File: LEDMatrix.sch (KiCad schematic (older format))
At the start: 80 parts

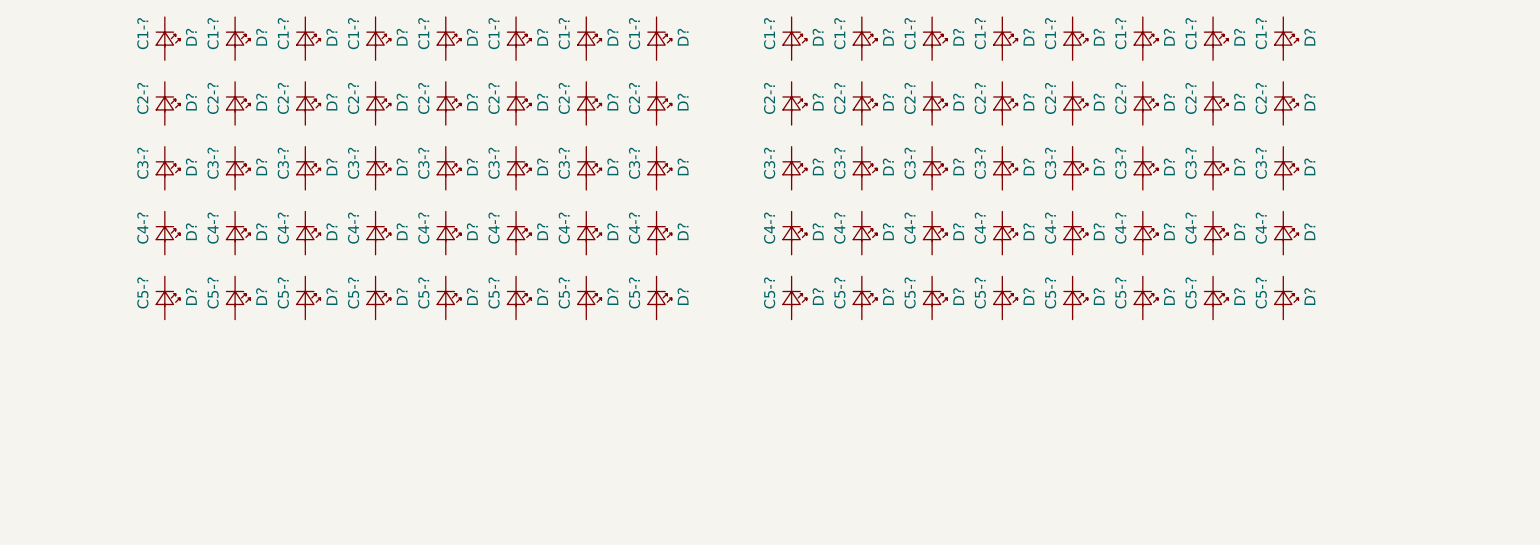
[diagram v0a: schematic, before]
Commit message: Place and annotate LED schematic components
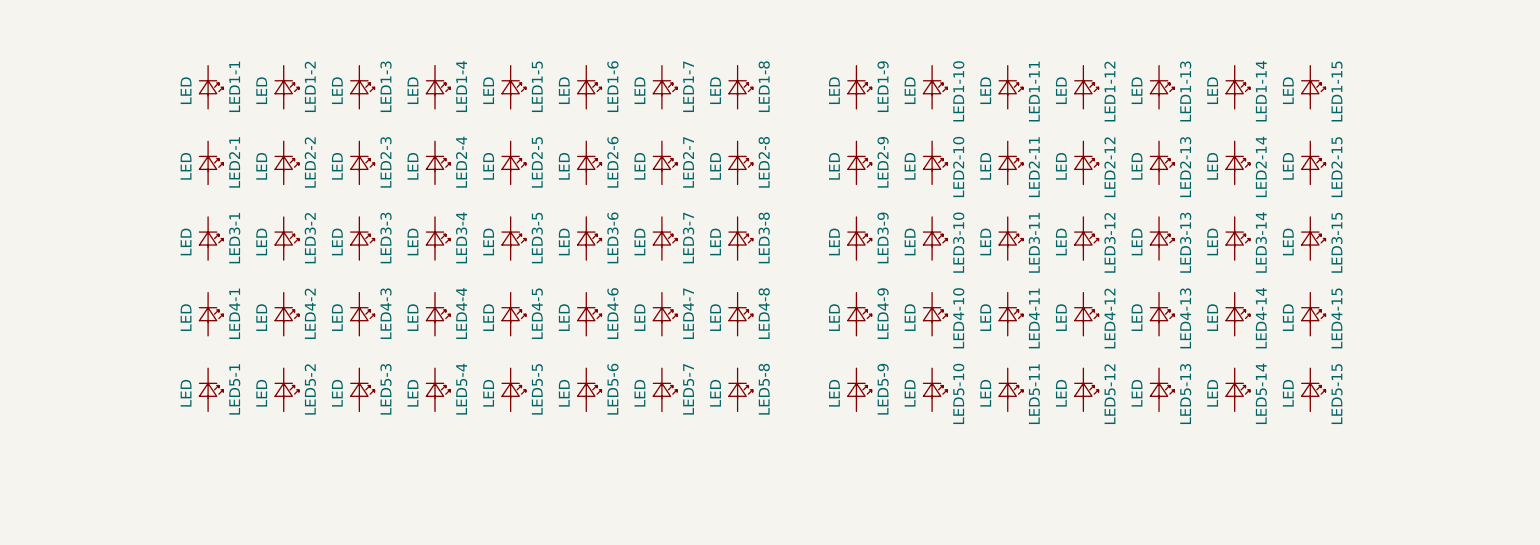
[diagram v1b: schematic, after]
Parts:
- removed D? (x16): C1-?, symbol LED_Small
- removed D? (x16): C2-?, symbol LED_Small
- removed D? (x16): C3-?, symbol LED_Small
- removed D? (x16): C4-?, symbol LED_Small
- removed D? (x16): C5-?, symbol LED_Small
- added LED1-1, LED1-10, LED1-11, LED1-12, LED1-13, LED1-14, LED1-15, LED1-2, LED1-3, LED1-4, LED1-5, LED1-6, LED1-7, LED1-8, LED1-9, LED2-1, LED2-10, LED2-11, LED2-12, LED2-13, LED2-14, LED2-15, LED2-2, LED2-3, LED2-4, LED2-5, LED2-6, LED2-7, LED2-8, LED2-9, LED3-1, LED3-10, LED3-11, LED3-12, LED3-13, LED3-14, LED3-15, LED3-2, LED3-3, LED3-4, LED3-5, LED3-6, LED3-7, LED3-8, LED3-9, LED4-1, LED4-10, LED4-11, LED4-12, LED4-13, LED4-14, LED4-15, LED4-2, LED4-3, LED4-4, LED4-5, LED4-6, LED4-7, LED4-8, LED4-9, LED5-1, LED5-10, LED5-11, LED5-12, LED5-13, LED5-14, LED5-15, LED5-2, LED5-3, LED5-4, LED5-5, LED5-6, LED5-7, LED5-8, LED5-9: LED, symbol LED_Small

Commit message: Wire lefthand matrix schematic
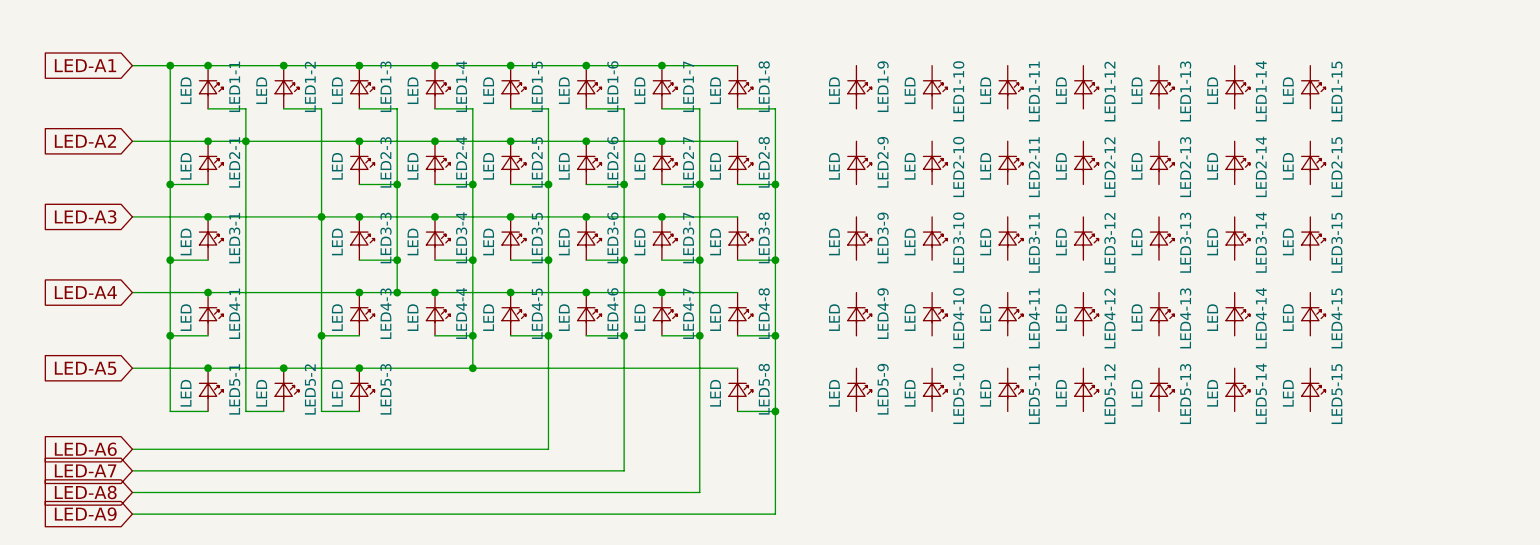
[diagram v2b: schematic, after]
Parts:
- removed LED2-2, LED3-2, LED4-2, LED5-4, LED5-5, LED5-6, LED5-7: LED, symbol LED_Small
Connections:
- net LED-A1: now reaches LED1-1.1 (K)
- net LED-A1: now also LED1-2.1 (K), LED1-3.1 (K), LED1-4.1 (K), LED1-5.1 (K), LED1-6.1 (K), LED1-7.1 (K), LED1-8.1 (K), LED2-1.2 (A), LED3-1.2 (A), LED4-1.2 (A), LED5-1.2 (A)
- net LED-A2: now reaches LED1-1.2 (A)
- net LED-A2: now also LED2-1.1 (K), LED2-3.1 (K), LED2-4.1 (K), LED2-5.1 (K), LED2-6.1 (K), LED2-7.1 (K), LED2-8.1 (K), LED5-2.2 (A)
- net LED-A3: now reaches LED1-2.2 (A)
- net LED-A3: now also LED3-1.1 (K), LED3-3.1 (K), LED3-4.1 (K), LED3-5.1 (K), LED3-6.1 (K), LED3-7.1 (K), LED3-8.1 (K), LED4-3.2 (A), LED5-3.2 (A)
- net LED-A4: now reaches LED1-3.2 (A)
- net LED-A4: now also LED2-3.2 (A), LED3-3.2 (A), LED4-1.1 (K), LED4-3.1 (K), LED4-4.1 (K), LED4-5.1 (K), LED4-6.1 (K), LED4-7.1 (K), LED4-8.1 (K)
- net LED-A5: now reaches LED1-4.2 (A)
- net LED-A5: now also LED2-4.2 (A), LED3-4.2 (A), LED4-4.2 (A), LED5-1.1 (K), LED5-2.1 (K), LED5-3.1 (K), LED5-8.1 (K)
- net LED-A6: now reaches LED1-5.2 (A)
- net LED-A6: now also LED2-5.2 (A), LED3-5.2 (A), LED4-5.2 (A)
- net LED-A7: now reaches LED1-6.2 (A)
- net LED-A7: now also LED2-6.2 (A), LED3-6.2 (A), LED4-6.2 (A)
- net LED-A8: now reaches LED1-7.2 (A)
- net LED-A8: now also LED2-7.2 (A), LED3-7.2 (A), LED4-7.2 (A)
- net LED-A9: now reaches LED1-8.2 (A)
- net LED-A9: now also LED2-8.2 (A), LED3-8.2 (A), LED4-8.2 (A), LED5-8.2 (A)

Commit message: Wire righthand matrix
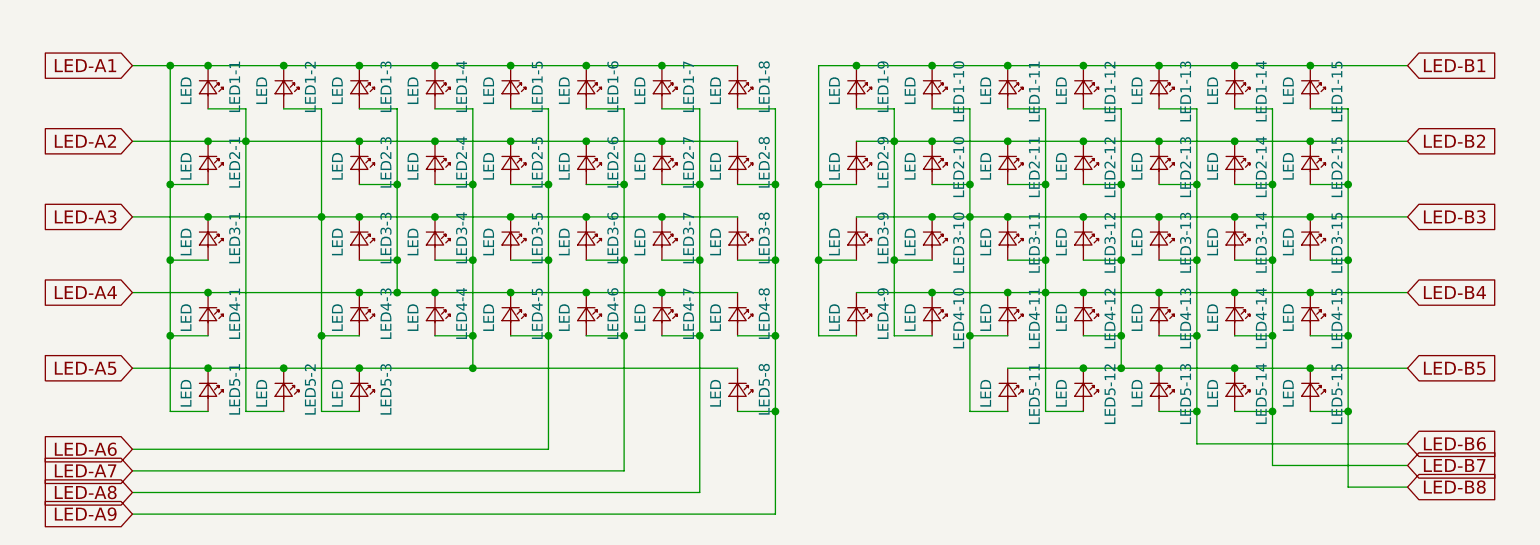
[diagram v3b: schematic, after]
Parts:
- removed LED5-10, LED5-9: LED, symbol LED_Small
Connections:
- net LED-B1: now reaches LED1-9.1 (K)
- net LED-B1: now also LED1-10.1 (K), LED1-11.1 (K), LED1-12.1 (K), LED1-13.1 (K), LED1-14.1 (K), LED1-15.1 (K), LED2-9.2 (A), LED3-9.2 (A), LED4-9.2 (A)
- net LED-B2: now reaches LED1-9.2 (A)
- net LED-B2: now also LED2-10.1 (K), LED2-11.1 (K), LED2-12.1 (K), LED2-13.1 (K), LED2-14.1 (K), LED2-15.1 (K), LED2-9.1 (K), LED3-10.2 (A), LED4-10.2 (A)
- net LED-B3: now reaches LED1-10.2 (A)
- net LED-B3: now also LED2-10.2 (A), LED3-10.1 (K), LED3-11.1 (K), LED3-12.1 (K), LED3-13.1 (K), LED3-14.1 (K), LED3-15.1 (K), LED3-9.1 (K), LED4-11.2 (A), LED5-11.2 (A)
- net LED-B4: now reaches LED1-11.2 (A)
- net LED-B4: now also LED2-11.2 (A), LED3-11.2 (A), LED4-10.1 (K), LED4-11.1 (K), LED4-12.1 (K), LED4-13.1 (K), LED4-14.1 (K), LED4-15.1 (K), LED4-9.1 (K), LED5-12.2 (A)
- net LED-B5: now reaches LED1-12.2 (A)
- net LED-B5: now also LED2-12.2 (A), LED3-12.2 (A), LED4-12.2 (A), LED5-11.1 (K), LED5-12.1 (K), LED5-13.1 (K), LED5-14.1 (K), LED5-15.1 (K)
- net LED-B6: now reaches LED1-13.2 (A)
- net LED-B6: now also LED2-13.2 (A), LED3-13.2 (A), LED4-13.2 (A), LED5-13.2 (A)
- net LED-B7: now reaches LED1-14.2 (A)
- net LED-B7: now also LED2-14.2 (A), LED3-14.2 (A), LED4-14.2 (A), LED5-14.2 (A)
- net LED-B8: now reaches LED1-15.2 (A)
- net LED-B8: now also LED2-15.2 (A), LED3-15.2 (A), LED4-15.2 (A), LED5-15.2 (A)
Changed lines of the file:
@@
-$EndComp
-$Comp
-L LED_Small LED5-9
-U 1 1 5A6E1441
-P 5200 3350
-F 0 "LED5-9" H 5075 3475 50  0000 L CNN
-F 1 "LED" H 5150 3250 50  0000 L CNN
-F 2 "" V 5200 3350 50  0001 C CNN
-F 3 "" V 5200 3350 50  0001 C CNN
-	1    5200 3350
-	0    1    1    0
-$EndComp
-$Comp
-L LED_Small LED5-10
-U 1 1 5A6E1447
-P 5550 3350
-F 0 "LED5-10" H 5425 3475 50  0000 L CNN
-F 1 "LED" H 5500 3250 50  0000 L CNN
-F 2 "" V 5550 3350 50  0001 C CNN
-F 3 "" V 5550 3350 50  0001 C CNN
-	1    5550 3350
-	0    1    1    0
 $EndComp
 $Comp
@@
 Text GLabel 1850 3250 0    60   Input ~ 0
 LED-A5
+Text GLabel 1850 3625 0    60   Input ~ 0
+LED-A6
+Text GLabel 1850 3725 0    60   Input ~ 0
+LED-A7
+Text GLabel 1850 3825 0    60   Input ~ 0
+LED-A8
+Text GLabel 1850 3925 0    60   Input ~ 0
+LED-A9
+Text GLabel 7750 1850 2    60   Input ~ 0
+LED-B1
+Text GLabel 7750 2200 2    60   Input ~ 0
+LED-B2
+Text GLabel 7750 2550 2    60   Input ~ 0
+LED-B3
+Text GLabel 7750 2900 2    60   Input ~ 0
+LED-B4
+Text GLabel 7750 3250 2    60   Input ~ 0
+LED-B5
 Wire Wire Line
 	1850 1850 4650 1850
@@
 	3425 2050 3250 2050
 Connection ~ 3425 2400
-Text GLabel 1850 3625 0    60   Input ~ 0
-LED-A6
 Wire Wire Line
 	3775 3625 1850 3625
@@
 	3775 2050 3600 2050
 Connection ~ 3775 2400
-Text GLabel 1850 3725 0    60   Input ~ 0
-LED-A7
 Wire Wire Line
 	4125 3725 1850 3725
@@
 	4125 2050 3950 2050
 Connection ~ 4125 2400
-Text GLabel 1850 3825 0    60   Input ~ 0
-LED-A8
 Wire Wire Line
 	4475 3825 1850 3825
@@
 	4475 2050 4300 2050
 Connection ~ 4475 2400
-Text GLabel 1850 3925 0    60   Input ~ 0
-LED-A9
 Wire Wire Line
 	4825 3925 1850 3925
@@
 	4825 2050 4650 2050
 Connection ~ 4825 2400
+Wire Wire Line
+	5025 1850 7750 1850
+Connection ~ 5550 1850
+Connection ~ 5900 1850
+Connection ~ 6250 1850
+Connection ~ 6600 1850
+Connection ~ 6950 1850
+Connection ~ 7300 1850
+Wire Wire Line
+	5200 2200 7750 2200
+Connection ~ 5550 2200
+Connection ~ 5900 2200
+Connection ~ 6250 2200
+Connection ~ 6600 2200
+Connection ~ 6950 2200
+Connection ~ 7300 2200
+Wire Wire Line
+	5200 2550 7750 2550
+Connection ~ 5550 2550
+Connection ~ 5900 2550
+Connection ~ 6250 2550
+Connection ~ 6600 2550
+Connection ~ 6950 2550
+Connection ~ 7300 2550
+Wire Wire Line
+	5200 2900 7750 2900
+Connection ~ 5550 2900
+Connection ~ 5900 2900
+Connection ~ 6250 2900
+Connection ~ 6600 2900
+Connection ~ 6950 2900
+Connection ~ 7300 2900
+Wire Wire Line
+	5900 3250 7750 3250
+Connection ~ 6250 3250
+Connection ~ 6600 3250
+Connection ~ 6950 3250
+Connection ~ 7300 3250
+Wire Wire Line
+	5025 1850 5025 3100
+Wire Wire Line
+	5025 2400 5200 2400
+Connection ~ 5200 1850
+Wire Wire Line
+	5025 2750 5200 2750
+Connection ~ 5025 2400
+Wire Wire Line
+	5025 3100 5200 3100
+Connection ~ 5025 2750
+Wire Wire Line
+	5375 2050 5375 3100
+Wire Wire Line
+	5375 2050 5200 2050
+Connection ~ 5375 2200
+Wire Wire Line
+	5375 2750 5550 2750
+Wire Wire Line
+	5375 3100 5550 3100
+Connection ~ 5375 2750
+Wire Wire Line
+	5725 2050 5725 3450
+Wire Wire Line
+	5725 2400 5550 2400
+Connection ~ 5725 2550
+Wire Wire Line
+	5725 2050 5550 2050
+Connection ~ 5725 2400
+Wire Wire Line
+	5725 3100 5900 3100
+Wire Wire Line
+	5725 3450 5900 3450
+Connection ~ 5725 3100
+Wire Wire Line
+	6075 2050 6075 3450
+Wire Wire Line
+	6075 2750 5900 2750
+Connection ~ 6075 2900
+Wire Wire Line
+	6075 2400 5900 2400
+Connection ~ 6075 2750
+Wire Wire Line
+	6075 2050 5900 2050
+Connection ~ 6075 2400
+Wire Wire Line
+	6075 3450 6250 3450
+Wire Wire Line
+	6250 2050 6425 2050
+Wire Wire Line
+	6425 2050 6425 3250
+Connection ~ 6425 3250
+Wire Wire Line
+	6250 3100 6425 3100
+Connection ~ 6425 3100
+Wire Wire Line
+	6425 2750 6250 2750
+Connection ~ 6425 2750
+Wire Wire Line
+	6250 2400 6425 2400
+Connection ~ 6425 2400
+Wire Wire Line
+	6600 3100 6775 3100
+Wire Wire Line
+	6775 2050 6775 3600
+Wire Wire Line
+	6775 2750 6600 2750
+Wire Wire Line
+	6775 3450 6600 3450
+Connection ~ 6775 3100
+Wire Wire Line
+	6775 2400 6600 2400
+Connection ~ 6775 2750
+Wire Wire Line
+	6600 2050 6775 2050
+Connection ~ 6775 2400
+Wire Wire Line
+	6950 2050 7125 2050
+Wire Wire Line
+	7125 2050 7125 3700
+Wire Wire Line
+	7125 2400 6950 2400
+Wire Wire Line
+	7125 2750 6950 2750
+Connection ~ 7125 2400
+Wire Wire Line
+	7125 3100 6950 3100
+Connection ~ 7125 2750
+Wire Wire Line
+	7125 3450 6950 3450
+Connection ~ 7125 3100
+Wire Wire Line
+	7300 2050 7475 2050
+Wire Wire Line
+	7475 2050 7475 3800
+Wire Wire Line
+	7475 2400 7300 2400
+Wire Wire Line
+	7475 2750 7300 2750
+Connection ~ 7475 2400
+Wire Wire Line
+	7475 3100 7300 3100
+Connection ~ 7475 2750
+Wire Wire Line
+	7475 3450 7300 3450
+Connection ~ 7475 3100
+Wire Wire Line
+	6775 3600 7750 3600
+Connection ~ 6775 3450
+Text GLabel 7750 3600 2    60   Input ~ 0
+LED-B6
+Text GLabel 7750 3700 2    60   Input ~ 0
+LED-B7
+Wire Wire Line
+	7125 3700 7750 3700
+Connection ~ 7125 3450
+Text GLabel 7750 3800 2    60   Input ~ 0
+LED-B8
+Wire Wire Line
+	7475 3800 7750 3800
+Connection ~ 7475 3450
 $EndSCHEMATC

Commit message: Assign footprints
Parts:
- LED1-1, LED1-10, LED1-11, LED1-12, LED1-13, LED1-14, LED1-15, LED1-2, LED1-3, LED1-4, LED1-5, LED1-6, LED1-7, LED1-8, LED1-9, LED2-1, LED2-10, LED2-11, LED2-12, LED2-13, LED2-14, LED2-15, LED2-3, LED2-4, LED2-5, LED2-6, LED2-7, LED2-8, LED2-9, LED3-1, LED3-10, LED3-11, LED3-12, LED3-13, LED3-14, LED3-15, LED3-3, LED3-4, LED3-5, LED3-6, LED3-7, LED3-8, LED3-9, LED4-1, LED4-10, LED4-11, LED4-12, LED4-13, LED4-14, LED4-15, LED4-3, LED4-4, LED4-5, LED4-6, LED4-7, LED4-8, LED4-9, LED5-1, LED5-11, LED5-12, LED5-13, LED5-14, LED5-15, LED5-2, LED5-3, LED5-8: footprint (none) -> MX_Alps_Hybrid:LED

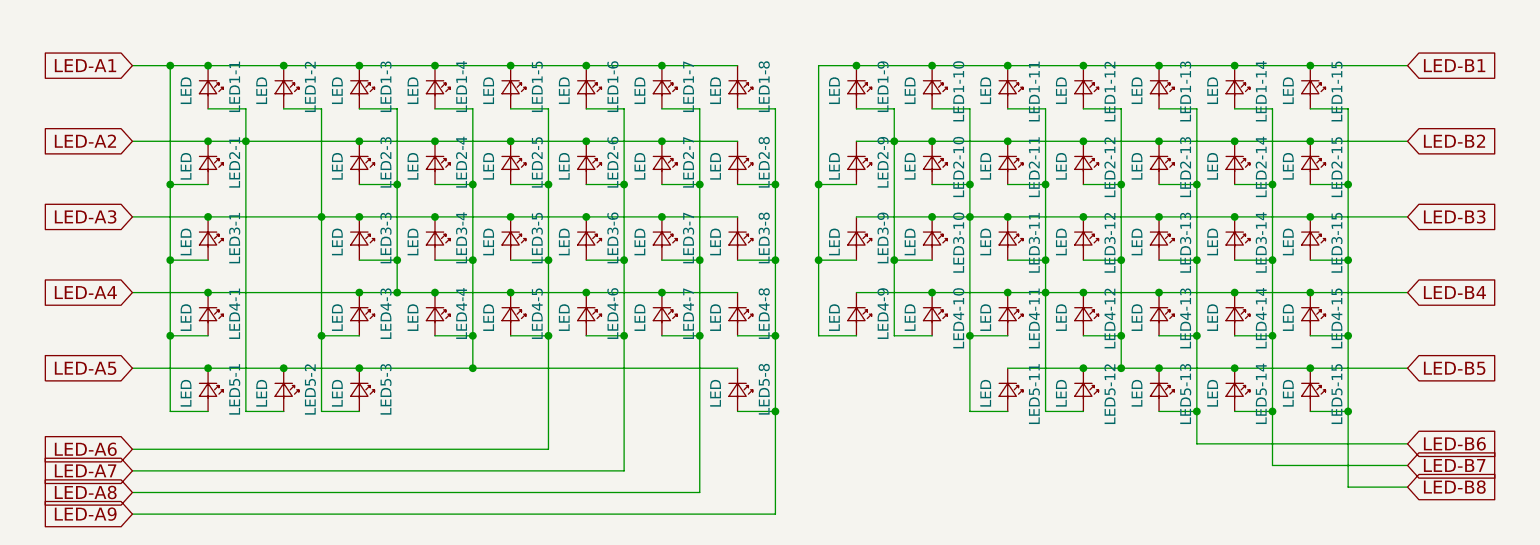
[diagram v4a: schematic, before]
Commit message: Add lefthand compat LEDs
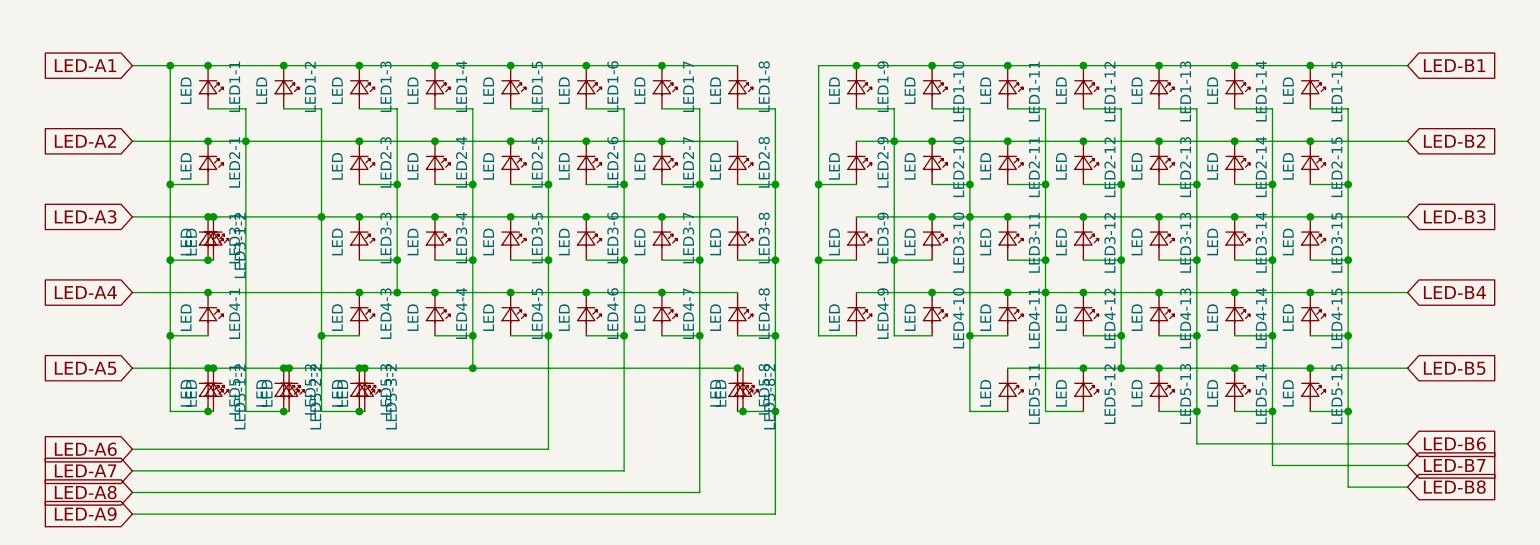
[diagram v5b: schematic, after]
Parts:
- added LED3-1-2, LED5-1-2, LED5-2-2, LED5-3-2: LED, MX_Alps_Hybrid:LED-FLIPPED, symbol LED_Small
- added LED5-8-2: LED, MX_Alps_Hybrid:LED, symbol LED_Small
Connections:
- net LED-A1: now also LED3-1-2.2 (A), LED5-1-2.2 (A)
- net LED-A2: now also LED5-2-2.2 (A)
- net LED-A3: now also LED3-1-2.1 (K), LED5-3-2.2 (A)
- net LED-A5: now also LED5-1-2.1 (K), LED5-2-2.1 (K), LED5-3-2.1 (K), LED5-8-2.1 (K)
- net LED-A9: now also LED5-8-2.2 (A)
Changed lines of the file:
@@
 Connection ~ 3250 2550
 Connection ~ 2900 2550
-Connection ~ 2200 2550
 Wire Wire Line
 	1850 2900 4650 2900
@@
 Connection ~ 2200 2900
 Wire Wire Line
-	1850 3250 4650 3250
-Connection ~ 2900 3250
-Connection ~ 2550 3250
-Connection ~ 2200 3250
+	1850 3250 4675 3250
 Wire Wire Line
 	2025 1850 2025 3450
@@
 Connection ~ 2025 1850
 Wire Wire Line
-	2025 2750 2200 2750
+	2025 2750 2225 2750
 Connection ~ 2025 2400
 Wire Wire Line
@@
 Connection ~ 2025 2750
 Wire Wire Line
-	2025 3450 2200 3450
+	2025 3450 2225 3450
 Connection ~ 2025 3100
 Wire Wire Line
@@
 Connection ~ 2375 2200
 Wire Wire Line
-	2375 3450 2550 3450
+	2375 3450 2575 3450
 Wire Wire Line
 	2725 2050 2725 3450
@@
 	2725 3100 2900 3100
 Wire Wire Line
-	2725 3450 2900 3450
+	2725 3450 2925 3450
 Connection ~ 2725 3100
 Wire Wire Line
@@
 	7475 3800 7750 3800
 Connection ~ 7475 3450
+$Comp
+L LED_Small LED5-1-2
+U 1 1 5A6D85C3
+P 2225 3350
+F 0 "LED5-1-2" H 2100 3475 50  0000 L CNN
+F 1 "LED" H 2175 3250 50  0000 L CNN
+F 2 "MX_Alps_Hybrid:LED-FLIPPED" V 2225 3350 50  0001 C CNN
+F 3 "" V 2225 3350 50  0001 C CNN
+	1    2225 3350
+	0    1    1    0
+$EndComp
+$Comp
+L LED_Small LED5-2-2
+U 1 1 5A6D8749
+P 2575 3350
+F 0 "LED5-2-2" H 2450 3475 50  0000 L CNN
+F 1 "LED" H 2525 3250 50  0000 L CNN
+F 2 "MX_Alps_Hybrid:LED-FLIPPED" V 2575 3350 50  0001 C CNN
+F 3 "" V 2575 3350 50  0001 C CNN
+	1    2575 3350
+	0    1    1    0
+$EndComp
+$Comp
+L LED_Small LED5-3-2
+U 1 1 5A6D88EC
+P 2925 3350
+F 0 "LED5-3-2" H 2800 3475 50  0000 L CNN
+F 1 "LED" H 2875 3250 50  0000 L CNN
+F 2 "MX_Alps_Hybrid:LED-FLIPPED" V 2925 3350 50  0001 C CNN
+F 3 "" V 2925 3350 50  0001 C CNN
+	1    2925 3350
+	0    1    1    0
+$EndComp
+Connection ~ 2900 3250
+Connection ~ 2550 3250
+Connection ~ 2200 3250
+$Comp
+L LED_Small LED3-1-2
+U 1 1 5A6D99E6
+P 2225 2650
+F 0 "LED3-1-2" H 2100 2775 50  0000 L CNN
+F 1 "LED" H 2175 2550 50  0000 L CNN
+F 2 "MX_Alps_Hybrid:LED-FLIPPED" V 2225 2650 50  0001 C CNN
+F 3 "" V 2225 2650 50  0001 C CNN
+	1    2225 2650
+	0    1    1    0
+$EndComp
+Connection ~ 2200 2550
+Connection ~ 2225 2550
+Connection ~ 2200 2750
+Connection ~ 2200 3450
+Connection ~ 2225 3250
+Connection ~ 2550 3450
+Connection ~ 2575 3250
+Connection ~ 2900 3450
+Connection ~ 2925 3250
+$Comp
+L LED_Small LED5-8-2
+U 1 1 5A6DC14A
+P 4675 3350
+F 0 "LED5-8-2" H 4550 3475 50  0000 L CNN
+F 1 "LED" H 4625 3250 50  0000 L CNN
+F 2 "MX_Alps_Hybrid:LED" V 4675 3350 50  0001 C CNN
+F 3 "" V 4675 3350 50  0001 C CNN
+	1    4675 3350
+	0    1    1    0
+$EndComp
+Connection ~ 4650 3250
+Connection ~ 4675 3450
 $EndSCHEMATC
